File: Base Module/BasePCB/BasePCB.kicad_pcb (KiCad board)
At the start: 2 copper layers, 75.4 x 38.1 mm, 24 parts, among them J1 USB_A, SW1 SW_Push, U1 ATmega32U4-A, Y1 Crystal_GND24_Small

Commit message: Updated wiring
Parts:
- moved C4 0.81 mm to (177.8, 133.2)
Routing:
- net GND: track 46.1 -> 98.1 mm, vias 0 -> 2
- net COL0: track 0.00 -> 23.5 mm
- net ROW0: track 0.00 -> 22.9 mm
- net ROW1: track 0.00 -> 19.8 mm
- net +5V: track 25.9 -> 44.3 mm
- net Net-(R1-Pad2): track 0.00 -> 17.5 mm
- net Net-(C3-Pad2): track 0.00 -> 14.6 mm
- net Net-(R2-Pad2): track 0.00 -> 11.4 mm
- net Net-(R3-Pad2): track 13.3 -> 22.0 mm
- net Net-(R4-Pad1): track 0.00 -> 8.75 mm
- net Net-(D3-Pad2): track 0.00 -> 7.23 mm
- net Net-(D1-Pad2): track 0.00 -> 7.23 mm
- net Net-(D2-Pad2): track 0.00 -> 6.92 mm
- net Net-(D4-Pad2): track 0.00 -> 6.02 mm
- net Net-(C2-Pad1): track 0.00 -> 3.70 mm

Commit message: Updated wiring
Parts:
- moved C5 0.79 mm to (171.4, 117.5)
- moved C6 0.79 mm to (165.1, 117.5)
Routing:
- net GND: track 98.1 -> 146.9 mm, vias 2 -> 7
- net ROW1: track 19.8 -> 62.7 mm, vias 0 -> 2
- net +5V: track 44.3 -> 84.6 mm, vias 0 -> 4
- net COL1: track 0.00 -> 40.2 mm, vias 0 -> 4
- net Net-(C2-Pad1): track 3.70 -> 29.5 mm
- net ROW0: track 22.9 -> 48.2 mm
- net COL0: track 23.5 -> 47.6 mm, vias 0 -> 2

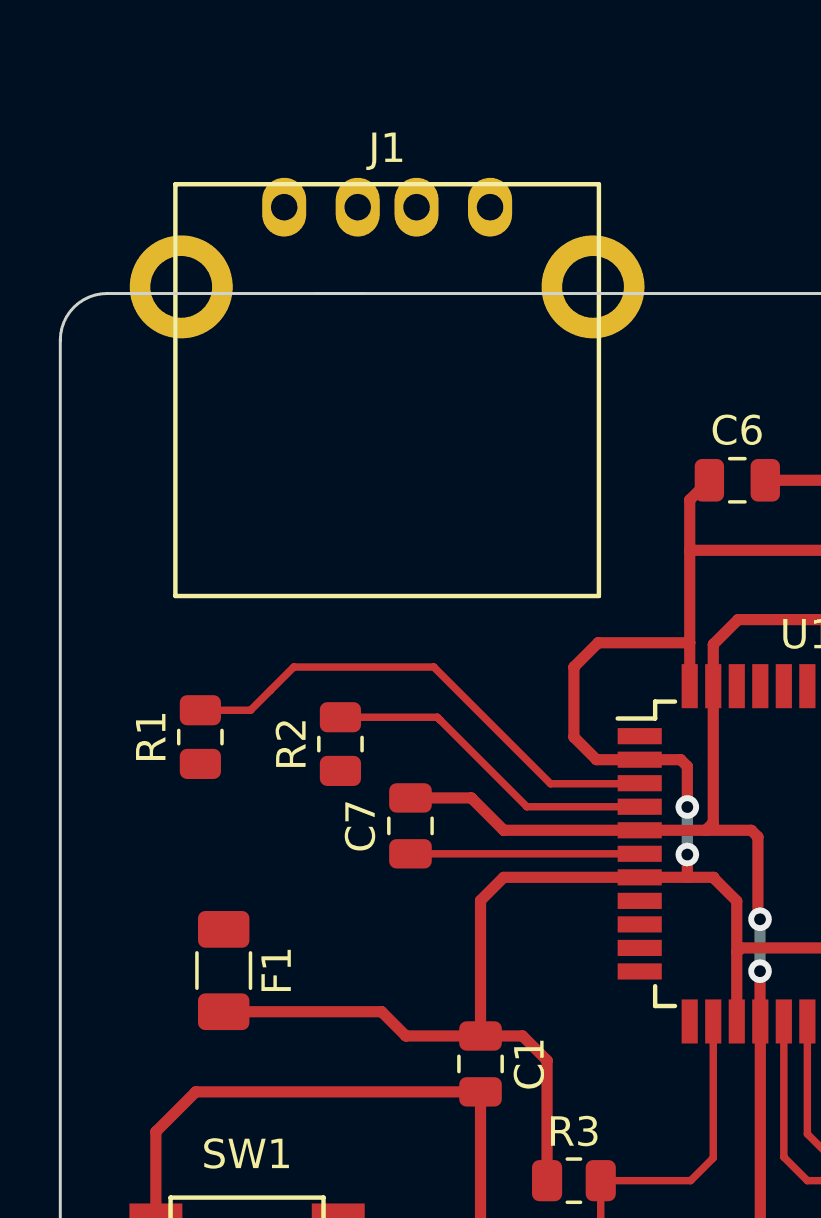
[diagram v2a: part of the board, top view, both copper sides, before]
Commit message: Finished base module wiring
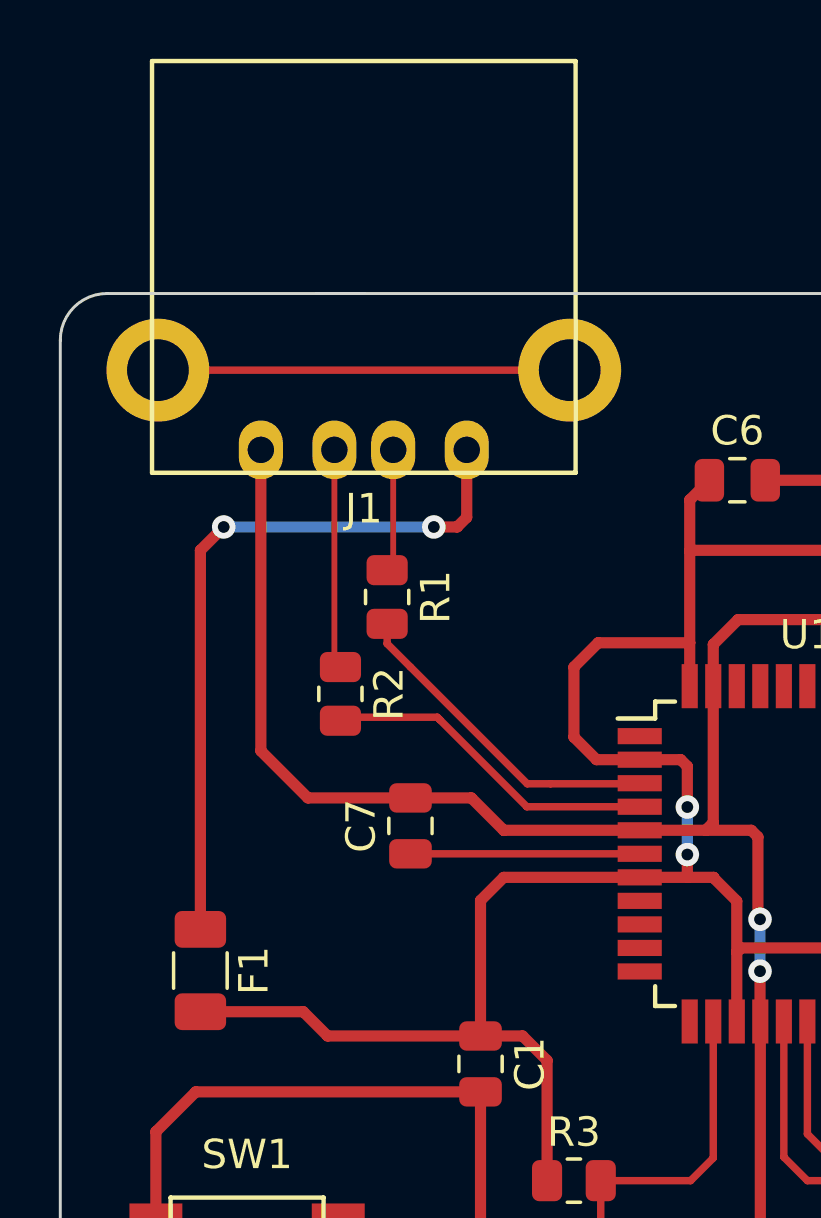
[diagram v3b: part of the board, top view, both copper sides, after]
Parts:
- moved J1 8.29 mm to (152.4, 116.4), turned to 180 degrees
- moved R1 7.94 mm to (153.2, 121.4), turned to -90 degrees
- moved R2 1.71 mm to (151.6, 124.7), turned to -90 degrees
- moved F1 0.79 mm to (146.8, 134.1)
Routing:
- net VCC: track 0.00 -> 24.7 mm, vias 0 -> 2
- net GND: track 146.9 -> 162.9 mm
- net unconnected-(J1-Pad5): track 0.00 -> 14.0 mm
- net D+: track 0.00 -> 7.47 mm
- net Net-(R1-Pad2): track 17.5 -> 11.5 mm
- net D-: track 0.00 -> 4.41 mm
- net +5V: track 84.6 -> 85.4 mm

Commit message: Added new components to PCB
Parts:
- added D10: D_Small, Diode_SMD:D_SOD-123, F.Cu at (39.5, 121.6)
- added D11: D_Small, Diode_SMD:D_SOD-123, F.Cu at (28.0, 121.6)
- added D12: D_Small, Diode_SMD:D_SOD-123, F.Cu at (68.2, 115.3)
- added D13: D_Small, Diode_SMD:D_SOD-123, F.Cu at (56.7, 122.0)
- added D14: D_Small, Diode_SMD:D_SOD-123, F.Cu at (62.5, 122.0)
- added D15: D_Small, Diode_SMD:D_SOD-123, F.Cu at (91.2, 105.3)
- added D16: D_Small, Diode_SMD:D_SOD-123, F.Cu at (51.0, 108.6)
- added D17: D_Small, Diode_SMD:D_SOD-123, F.Cu at (74.0, 112.0)
- added D18: D_Small, Diode_SMD:D_SOD-123, F.Cu at (62.5, 115.3)
- added D19: D_Small, Diode_SMD:D_SOD-123, F.Cu at (45.2, 118.7)
- added D20: D_Small, Diode_SMD:D_SOD-123, F.Cu at (62.5, 118.7)
- added D21: D_Small, Diode_SMD:D_SOD-123, F.Cu at (85.5, 108.6)
- added D22: D_Small, Diode_SMD:D_SOD-123, F.Cu at (97.0, 105.3)
- added D23: D_Small, Diode_SMD:D_SOD-123, F.Cu at (56.7, 108.6)
- added D24: D_Small, Diode_SMD:D_SOD-123, F.Cu at (45.2, 112.0)
- added D25: D_Small, Diode_SMD:D_SOD-123, F.Cu at (62.5, 105.3)
- added D26: D_Small, Diode_SMD:D_SOD-123, F.Cu at (85.5, 112.0)
- added D27: D_Small, Diode_SMD:D_SOD-123, F.Cu at (79.7, 115.3)
- added D28: D_Small, Diode_SMD:D_SOD-123, F.Cu at (33.7, 118.3)
- added D29: D_Small, Diode_SMD:D_SOD-123, F.Cu at (68.2, 112.0)
- added D30: D_Small, Diode_SMD:D_SOD-123, F.Cu at (74.0, 105.3)
- added D31: D_Small, Diode_SMD:D_SOD-123, F.Cu at (74.0, 108.6)
- added D32: D_Small, Diode_SMD:D_SOD-123, F.Cu at (44.4, 105.3)
- added D33: D_Small, Diode_SMD:D_SOD-123, F.Cu at (74.0, 115.3)
- added D34: D_Small, Diode_SMD:D_SOD-123, F.Cu at (22.2, 114.9)
- added D35: D_Small, Diode_SMD:D_SOD-123, F.Cu at (51.0, 112.0)
- added D36: D_Small, Diode_SMD:D_SOD-123, F.Cu at (28.0, 114.9)
- added D37: D_Small, Diode_SMD:D_SOD-123, F.Cu at (56.7, 112.0)
- added D38: D_Small, Diode_SMD:D_SOD-123, F.Cu at (16.5, 114.9)
- added D39: D_Small, Diode_SMD:D_SOD-123, F.Cu at (39.5, 118.3)
- added D40: D_Small, Diode_SMD:D_SOD-123, F.Cu at (45.2, 122.0)
- added D41: D_Small, Diode_SMD:D_SOD-123, F.Cu at (51.0, 122.0)
- added D42: D_Small, Diode_SMD:D_SOD-123, F.Cu at (68.2, 105.3)
- added D43: D_Small, Diode_SMD:D_SOD-123, F.Cu at (39.5, 114.9)
- added D44: D_Small, Diode_SMD:D_SOD-123, F.Cu at (62.5, 108.6)
- added D45: D_Small, Diode_SMD:D_SOD-123, F.Cu at (56.7, 105.3)
- added D46: D_Small, Diode_SMD:D_SOD-123, F.Cu at (79.7, 108.6)
- added D47: D_Small, Diode_SMD:D_SOD-123, F.Cu at (28.0, 118.3)
- added D48: D_Small, Diode_SMD:D_SOD-123, F.Cu at (68.2, 108.6)
- added D49: D_Small, Diode_SMD:D_SOD-123, F.Cu at (56.7, 115.3)
- added D5: D_Small, Diode_SMD:D_SOD-123, F.Cu at (22.2, 118.3)
- added D50: D_Small, Diode_SMD:D_SOD-123, F.Cu at (51.0, 115.3)
- added D51: D_Small, Diode_SMD:D_SOD-123, F.Cu at (85.5, 105.3)
- added D52: D_Small, Diode_SMD:D_SOD-123, F.Cu at (56.7, 118.7)
- added D53: D_Small, Diode_SMD:D_SOD-123, F.Cu at (45.2, 115.3)
- added D54: D_Small, Diode_SMD:D_SOD-123, F.Cu at (79.7, 112.0)
- added D55: D_Small, Diode_SMD:D_SOD-123, F.Cu at (16.5, 118.3)
- added D56: D_Small, Diode_SMD:D_SOD-123, F.Cu at (62.5, 112.0)
- added D57: D_Small, Diode_SMD:D_SOD-123, F.Cu at (91.2, 108.6)
- added D58: D_Small, Diode_SMD:D_SOD-123, F.Cu at (33.7, 121.6)
- added D59: D_Small, Diode_SMD:D_SOD-123, F.Cu at (33.7, 114.9)
- added D6: D_Small, Diode_SMD:D_SOD-123, F.Cu at (51.0, 105.3)
- added D60: D_Small, Diode_SMD:D_SOD-123, F.Cu at (51.0, 118.7)
- added D61: D_Small, Diode_SMD:D_SOD-123, F.Cu at (45.2, 108.6)
- added D7: D_Small, Diode_SMD:D_SOD-123, F.Cu at (22.2, 121.6)
- added D8: D_Small, Diode_SMD:D_SOD-123, F.Cu at (79.7, 105.3)
- added D9: D_Small, Diode_SMD:D_SOD-123, F.Cu at (16.5, 121.6)
- added J2: Conn_01x05_Female, Connector_JST:JST_PH_S5B-PH-K_1x05_P2.00mm_Horizontal, F.Cu at (30.5, 106.0)
- added J3: Conn_01x05_Male, Connector_JST:JST_PH_S5B-PH-K_1x05_P2.00mm_Horizontal, F.Cu at (16.6, 106.0)
- added MX_'1: MX-NoLED, MX_Alps_Hybrid:MX-1U-NoLED, F.Cu at (185.3, 12.7)
- added MX_,1: MX-NoLED, MX_Alps_Hybrid:MX-1U-NoLED, F.Cu at (205.5, 32.9)
- added MX_-1: MX-NoLED, MX_Alps_Hybrid:MX-1U-NoLED, F.Cu at (43.9, 53.1)
- added MX_.1: MX-NoLED, MX_Alps_Hybrid:MX-1U-NoLED, F.Cu at (185.3, -7.51)
- added MX_/1: MX-NoLED, MX_Alps_Hybrid:MX-1U-NoLED, F.Cu at (23.7, 73.3)
- added MX_0: MX-NoLED, MX_Alps_Hybrid:MX-1U-NoLED, F.Cu at (185.3, 53.1)
- added MX_2: MX-NoLED, MX_Alps_Hybrid:MX-1U-NoLED, F.Cu at (84.3, 93.5)
- added MX_3: MX-NoLED, MX_Alps_Hybrid:MX-1U-NoLED, F.Cu at (43.9, 12.7)
- added MX_4: MX-NoLED, MX_Alps_Hybrid:MX-1U-NoLED, F.Cu at (64.1, -7.51)
- added MX_5: MX-NoLED, MX_Alps_Hybrid:MX-1U-NoLED, F.Cu at (84.3, 53.1)
- added MX_6: MX-NoLED, MX_Alps_Hybrid:MX-1U-NoLED, F.Cu at (84.3, 12.7)
- added MX_7: MX-NoLED, MX_Alps_Hybrid:MX-1U-NoLED, F.Cu at (23.7, 53.1)
- added MX_8: MX-NoLED, MX_Alps_Hybrid:MX-1U-NoLED, F.Cu at (43.9, -7.51)
- added MX_9: MX-NoLED, MX_Alps_Hybrid:MX-1U-NoLED, F.Cu at (144.9, 32.9)
- added MX_;1: MX-NoLED, MX_Alps_Hybrid:MX-1U-NoLED, F.Cu at (23.7, 32.9)
- added MX_=1: MX-NoLED, MX_Alps_Hybrid:MX-1U-NoLED, F.Cu at (43.9, 32.9)
- added MX_A1: MX-NoLED, MX_Alps_Hybrid:MX-1U-NoLED, F.Cu at (165.1, 32.9)
- added MX_Alt1: MX-NoLED, MX_Alps_Hybrid:MX-1U-NoLED, F.Cu at (225.7, -7.51)
- added MX_Alt2: MX-NoLED, MX_Alps_Hybrid:MX-1U-NoLED, F.Cu at (64.1, 93.5)
- added MX_B1: MX-NoLED, MX_Alps_Hybrid:MX-1U-NoLED, F.Cu at (185.3, 32.9)
- added MX_Bksp1: MX-NoLED, MX_Alps_Hybrid:MX-1U-NoLED, F.Cu at (144.9, 73.3)
- added MX_C1: MX-NoLED, MX_Alps_Hybrid:MX-1U-NoLED, F.Cu at (104.5, -7.51)
- added MX_Caps1: MX-NoLED, MX_Alps_Hybrid:MX-1U-NoLED, F.Cu at (165.1, -7.51)
- added MX_Command1: MX-NoLED, MX_Alps_Hybrid:MX-1U-NoLED, F.Cu at (104.5, 53.1)
- added MX_Command2: MX-NoLED, MX_Alps_Hybrid:MX-1U-NoLED, F.Cu at (104.5, 32.9)
- added MX_Ctrl1: MX-NoLED, MX_Alps_Hybrid:MX-1U-NoLED, F.Cu at (144.9, -7.51)
- added MX_Ctrl2: MX-NoLED, MX_Alps_Hybrid:MX-1U-NoLED, F.Cu at (245.9, -7.51)
- added MX_D1: MX-NoLED, MX_Alps_Hybrid:MX-1U-NoLED, F.Cu at (84.3, 32.9)
- added MX_E1: MX-NoLED, MX_Alps_Hybrid:MX-1U-NoLED, F.Cu at (144.9, 12.7)
- added MX_Enter1: MX-NoLED, MX_Alps_Hybrid:MX-1U-NoLED, F.Cu at (124.7, 53.1)
- added MX_F1: MX-NoLED, MX_Alps_Hybrid:MX-1U-NoLED, F.Cu at (104.5, 73.3)
- added MX_FN1: MX-NoLED, MX_Alps_Hybrid:MX-1U-NoLED, F.Cu at (165.1, 53.1)
- added MX_G1: MX-NoLED, MX_Alps_Hybrid:MX-1U-NoLED, F.Cu at (64.1, 53.1)
- added MX_H1: MX-NoLED, MX_Alps_Hybrid:MX-1U-NoLED, F.Cu at (124.7, 32.9)
- added MX_I1: MX-NoLED, MX_Alps_Hybrid:MX-1U-NoLED, F.Cu at (144.9, 93.5)
- added MX_J1: MX-NoLED, MX_Alps_Hybrid:MX-1U-NoLED, F.Cu at (23.7, 93.5)
- added MX_K1: MX-NoLED, MX_Alps_Hybrid:MX-1U-NoLED, F.Cu at (124.7, 12.7)
- added MX_L1: MX-NoLED, MX_Alps_Hybrid:MX-1U-NoLED, F.Cu at (64.1, 73.3)
- added MX_M1: MX-NoLED, MX_Alps_Hybrid:MX-1U-NoLED, F.Cu at (64.1, 12.7)
- added MX_N1: MX-NoLED, MX_Alps_Hybrid:MX-1U-NoLED, F.Cu at (144.9, 53.1)
- added MX_O1: MX-NoLED, MX_Alps_Hybrid:MX-1U-NoLED, F.Cu at (124.7, 93.5)
- added MX_P1: MX-NoLED, MX_Alps_Hybrid:MX-1U-NoLED, F.Cu at (205.5, 12.7)
- added MX_R1: MX-NoLED, MX_Alps_Hybrid:MX-1U-NoLED, F.Cu at (124.7, -7.51)
- added MX_S1: MX-NoLED, MX_Alps_Hybrid:MX-1U-NoLED, F.Cu at (43.9, 73.3)
- added MX_Shift1: MX-NoLED, MX_Alps_Hybrid:MX-1U-NoLED, F.Cu at (84.3, 73.3)
- added MX_Shift2: MX-NoLED, MX_Alps_Hybrid:MX-1U-NoLED, F.Cu at (104.5, 12.7)
- added MX_Space1: MX-NoLED, MX_Alps_Hybrid:MX-1U-NoLED, F.Cu at (84.3, -7.51)
- added MX_T1: MX-NoLED, MX_Alps_Hybrid:MX-1U-NoLED, F.Cu at (23.7, 12.7)
- added MX_U1: MX-NoLED, MX_Alps_Hybrid:MX-1U-NoLED, F.Cu at (43.9, 93.5)
- added MX_V1: MX-NoLED, MX_Alps_Hybrid:MX-1U-NoLED, F.Cu at (124.7, 73.3)
- added MX_W1: MX-NoLED, MX_Alps_Hybrid:MX-1U-NoLED, F.Cu at (23.7, -7.51)
- added MX_X1: MX-NoLED, MX_Alps_Hybrid:MX-1U-NoLED, F.Cu at (165.1, 12.7)
- added MX_Y1: MX-NoLED, MX_Alps_Hybrid:MX-1U-NoLED, F.Cu at (64.1, 32.9)
- added MX_Z1: MX-NoLED, MX_Alps_Hybrid:MX-1U-NoLED, F.Cu at (225.7, 12.7)
- added MX_[1: MX-NoLED, MX_Alps_Hybrid:MX-1U-NoLED, F.Cu at (205.5, -7.51)
- added MX_\1: MX-NoLED, MX_Alps_Hybrid:MX-1U-NoLED, F.Cu at (104.5, 93.5)
- added MX_]1: MX-NoLED, MX_Alps_Hybrid:MX-1U-NoLED, F.Cu at (165.1, 73.3)
- added R5: 100, Resistor_SMD:R_0805_2012Metric, F.Cu at (67.6, 118.5)
- added R6: 100, Resistor_SMD:R_0805_2012Metric, F.Cu at (84.8, 115.1)
- renumbered MX3 to MX_1, MX1 to MX_Esc1, MX4 to MX_Q1, MX2 to MX_Tab1
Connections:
- U1 pad 10: unconnected-(U1-Pad10) -> COL3
- U1 pad 11: unconnected-(U1-Pad11) -> COL2
- U1 pad 12: unconnected-(U1-Pad12) -> ROW2
- U1 pad 18: unconnected-(U1-Pad18) -> COL10
- U1 pad 19: unconnected-(U1-Pad19) -> COL9
- U1 pad 20: unconnected-(U1-Pad20) -> COL8
- U1 pad 21: unconnected-(U1-Pad21) -> COL7
- U1 pad 22: unconnected-(U1-Pad22) -> ROW4
- U1 pad 25: unconnected-(U1-Pad25) -> COL6
- U1 pad 26: unconnected-(U1-Pad26) -> ROW3
- U1 pad 31: unconnected-(U1-Pad31) -> IN
- U1 pad 32: unconnected-(U1-Pad32) -> OUT
- U1 pad 39: unconnected-(U1-Pad39) -> COL13
- U1 pad 40: unconnected-(U1-Pad40) -> COL12
- U1 pad 41: unconnected-(U1-Pad41) -> COL11
- U1 pad 8: unconnected-(U1-Pad8) -> COL5
- U1 pad 9: unconnected-(U1-Pad9) -> COL4

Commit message: Started on schematic
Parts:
- moved MX_Tab1 402.0 mm to (-127.0, -101.6)
- moved D2 401.3 mm to (-119.1, -101.6)
- moved J1 400.7 mm to (-166.7, -126.0), turned to 0 degrees
- moved MX_Q1 397.5 mm to (-108.0, -101.6)
- moved D4 396.9 mm to (-100.0, -101.6)
- moved C2 393.2 mm to (-174.6, -54.8)
- moved Y1 391.9 mm to (-168.6, -54.3)
- moved C3 389.9 mm to (-162.7, -54.0)
- moved R1 383.7 mm to (-176.2, -75.4), turned to 90 degrees
- moved MX_Esc1 380.4 mm to (-98.4, -128.6)
- moved R2 380.0 mm to (-171.4, -75.4), turned to 90 degrees
- moved D1 379.8 mm to (-90.5, -128.7)
- moved MX_1 379.4 mm to (-79.4, -128.6)
- moved R3 378.9 mm to (-158.8, -64.3), turned to 90 degrees
- moved D3 378.9 mm to (-71.4, -128.6)
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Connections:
- J2 pad 1: VCC -> +5V
- J2 pad 2: unconnected-(J2-Pad2) -> VCC
- J3 pad 1: VCC -> +5V
- J3 pad 2: unconnected-(J3-Pad2) -> VCC
- R5 pad 1: IN -> OUT
- R6 pad 2: OUT -> IN
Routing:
- net GND: track 162.9 -> 0.00 mm, vias 7 -> 0
- net +5V: track 85.4 -> 0.00 mm, vias 4 -> 0
- net ROW1: track 62.7 -> 0.00 mm, vias 2 -> 0
- net ROW0: track 48.2 -> 0.00 mm
- net COL0: track 47.6 -> 0.00 mm, vias 2 -> 0
- net COL1: track 40.2 -> 0.00 mm, vias 4 -> 0
- net Net-(C2-Pad1): track 29.5 -> 0.00 mm
- net VCC: track 24.7 -> 0.00 mm, vias 2 -> 0
- net Net-(R3-Pad2): track 22.0 -> 0.00 mm
- net Net-(C3-Pad2): track 14.6 -> 0.00 mm
- net unconnected-(J1-Pad5): track 14.0 -> 0.00 mm
- net Net-(R1-Pad2): track 11.5 -> 0.00 mm
- net Net-(R2-Pad2): track 11.4 -> 0.00 mm
- net Net-(R4-Pad1): track 8.75 -> 0.00 mm
- net Net-(C7-Pad1): track 7.79 -> 0.00 mm
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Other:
- board outline removed

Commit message: Finished schematic placement, started wiring
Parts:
- moved D40 157.8 mm to (173.8, -52.4)
- moved MX_Ctrl2 157.8 mm to (165.9, -52.4)
- moved D35 153.2 mm to (150.0, -52.4)
- moved MX_FN1 153.2 mm to (142.1, -52.4)
- moved D30 149.3 mm to (127.0, -52.4)
- moved MX_Command2 149.3 mm to (119.1, -52.4)
- moved D25 143.9 mm to (102.4, -52.4)
- moved MX_Alt2 143.9 mm to (94.5, -52.4)
- moved D20 93.4 mm to (31.0, -52.4)
- moved MX_Space1 93.4 mm to (23.0, -52.4)
- moved J2 78.3 mm to (-143.7, -94.5), turned to -90 degrees
- moved R1 66.4 mm to (-126.7, -119.6), turned to -90 degrees
- moved D56 66.3 mm to (159.5, -71.4)
- moved MX_Shift2 66.3 mm to (151.6, -71.4)
- moved R5 65.8 mm to (-138.1, -90.5), turned to 180 degrees
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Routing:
- net COL11: track 0.00 -> 350.6 mm, vias 0 -> 2
- net ROW4: track 0.00 -> 340.9 mm
- net COL12: track 0.00 -> 340.5 mm, vias 0 -> 2
- net ROW0: track 0.00 -> 332.4 mm, vias 0 -> 29
- net COL13: track 0.00 -> 330.8 mm
- net ROW2: track 0.00 -> 328.2 mm, vias 0 -> 27
- net ROW1: track 0.00 -> 326.5 mm, vias 0 -> 26
- net ROW3: track 0.00 -> 324.9 mm, vias 0 -> 16
- net COL7: track 0.00 -> 200.1 mm
- net COL6: track 0.00 -> 196.8 mm
- net COL5: track 0.00 -> 193.2 mm
- net COL4: track 0.00 -> 185.7 mm
- net COL3: track 0.00 -> 131.3 mm
- net GND: track 0.00 -> 128.7 mm, vias 0 -> 2
- net COL1: track 0.00 -> 109.5 mm
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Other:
- board outline added: 321.5 x 95.3 mm

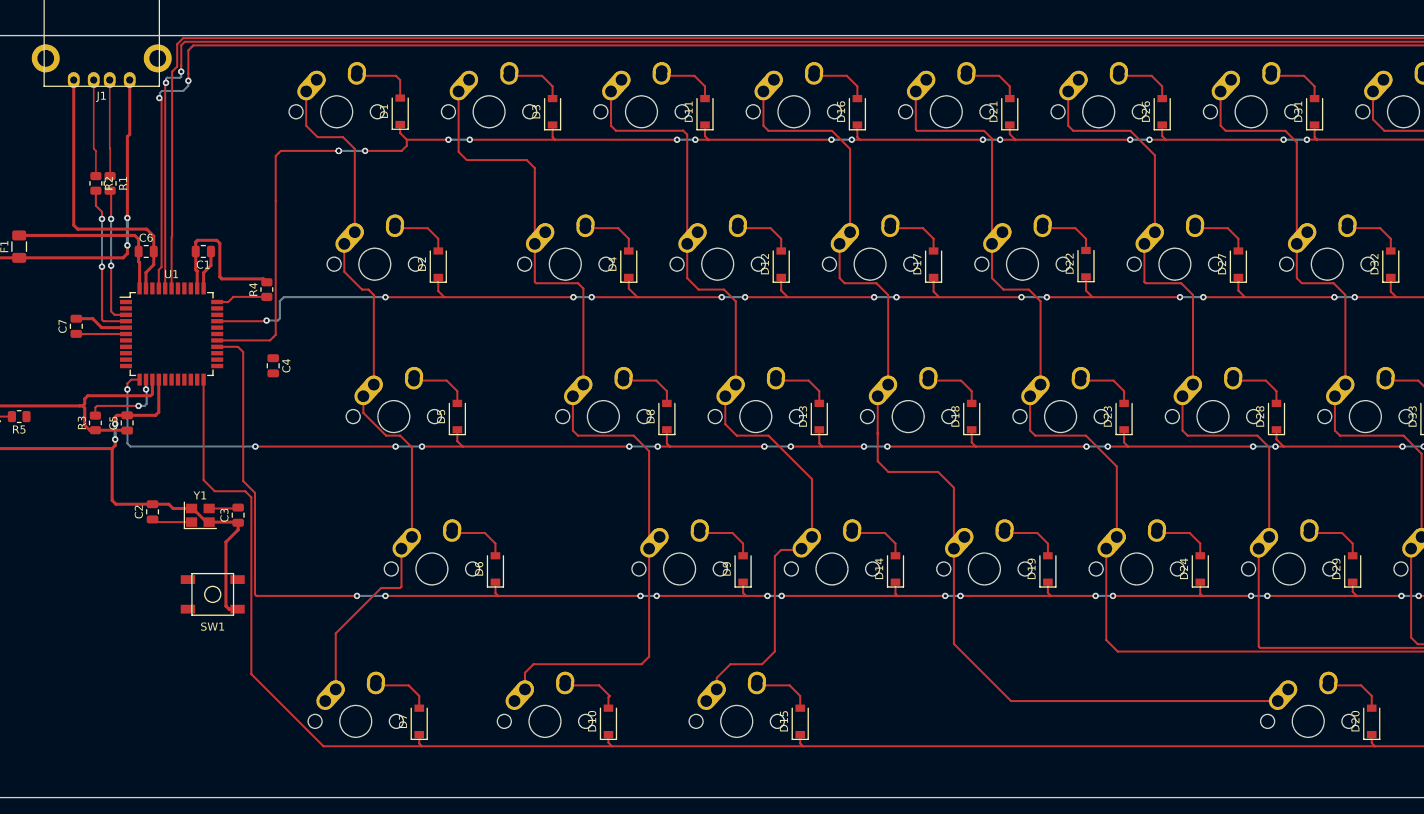
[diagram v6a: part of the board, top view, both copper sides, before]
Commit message: Continued wiring
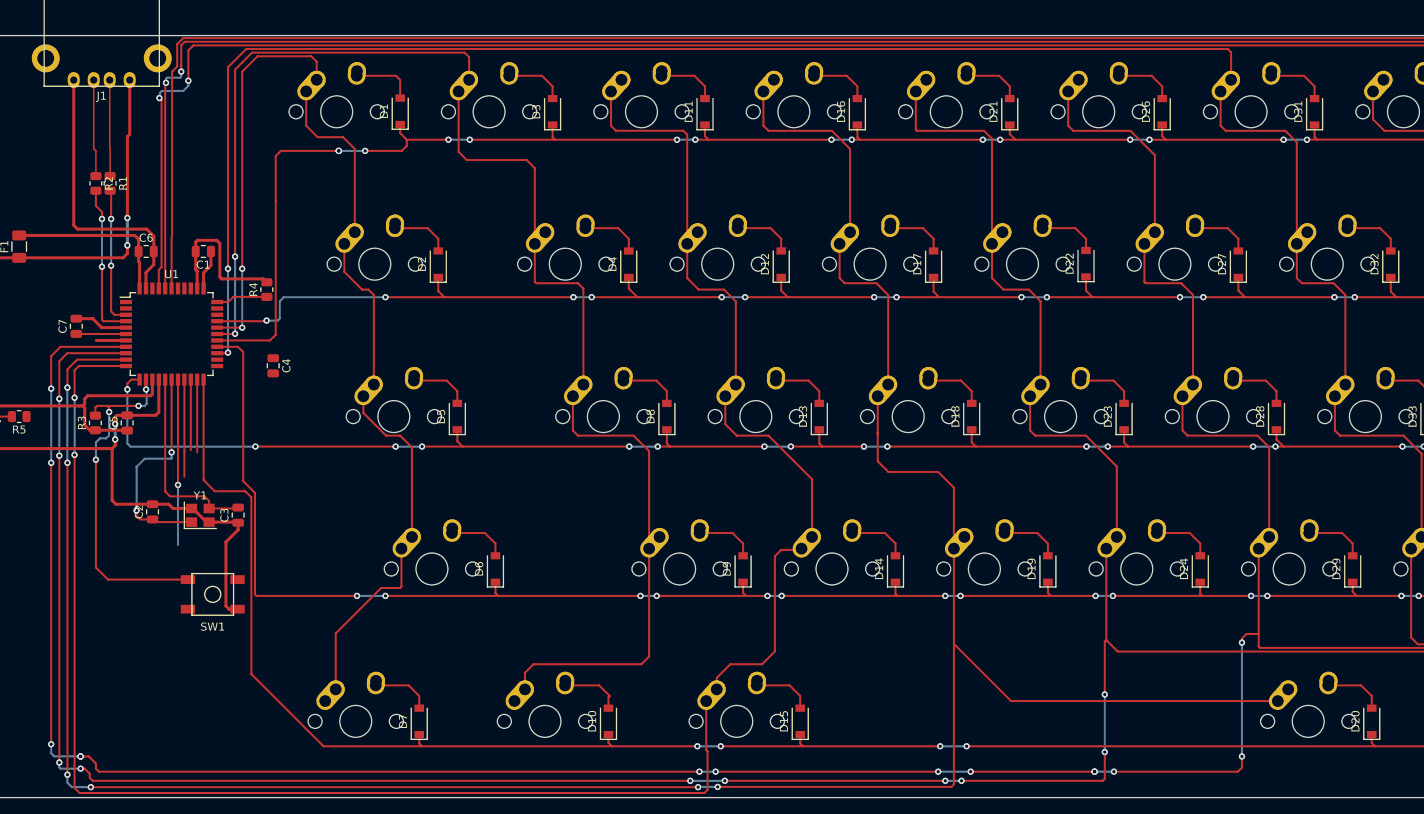
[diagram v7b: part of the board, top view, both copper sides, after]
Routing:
- net COL5: track 193.2 -> 421.5 mm, vias 0 -> 14
- net COL4: track 185.7 -> 394.5 mm, vias 0 -> 10
- net COL3: track 131.3 -> 319.6 mm, vias 0 -> 6
- net COL6: track 196.8 -> 363.8 mm, vias 0 -> 2
- net COL2: track 100.0 -> 249.6 mm, vias 0 -> 2
- net COL1: track 109.5 -> 178.1 mm, vias 0 -> 2
- net COL0: track 85.1 -> 132.9 mm, vias 0 -> 2
- net Net-(R3-Pad2): track 10.7 -> 44.3 mm, vias 2 -> 4
- net Net-(C2-Pad1): track 5.01 -> 28.0 mm, vias 0 -> 2
- net Net-(C3-Pad2): track 3.67 -> 24.6 mm
- net COL10: track 76.1 -> 96.8 mm, vias 0 -> 1
- net COL9: track 76.3 -> 88.5 mm
- net COL7: track 200.1 -> 209.1 mm
- net COL8: track 75.4 -> 84.2 mm
- net +5V: track 61.6 -> 65.3 mm
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
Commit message: Continued wiring
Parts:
- added J4: Conn_01x05_Female, Connector_JST:JST_PH_S5B-PH-K_1x05_P2.00mm_Horizontal, F.Cu at (27.0, -139.6)
- added J5: Conn_01x05_Female, Connector_JST:JST_PH_S5B-PH-K_1x05_P2.00mm_Horizontal, F.Cu at (19.1, -44.5)
- added R7: 100, Resistor_SMD:R_0805_2012Metric, F.Cu at (14.4, -139.7)
- added R8: 100, Resistor_SMD:R_0805_2012Metric, F.Cu at (23.8, -47.6)
- moved J1 4.21 mm to (-127.8, -136.8)
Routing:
- net COL10: track 96.8 -> 380.9 mm, vias 1 -> 14
- net COL9: track 88.5 -> 359.8 mm, vias 0 -> 17
- net COL8: track 84.2 -> 339.4 mm, vias 0 -> 7
- net GND: track 128.7 -> 371.4 mm, vias 2 -> 8
- net +5V: track 65.3 -> 306.3 mm, vias 0 -> 4
- net COL7: track 209.1 -> 385.3 mm, vias 0 -> 16
- net OUT: track 0.00 -> 163.9 mm, vias 0 -> 5
- net Net-(J4-Pad3): track 0.00 -> 9.96 mm
- net VCC: track 60.1 -> 64.3 mm
- net D+: track 12.1 -> 16.3 mm
- net D-: track 12.0 -> 16.2 mm
- net ROW4: track 340.9 -> 342.1 mm
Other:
- board size 321.5 x 95.3 mm -> 321.5 x 98.4 mm
